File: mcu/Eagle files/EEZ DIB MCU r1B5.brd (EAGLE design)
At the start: 139 x 70 mm, 197 parts, among them IC1 TPD4E001DRLR, IC10 TPS61169DCKR, IC11 TPD4E001DRLR, IC12 TPA6205A1DGN, IC13 TPD4E001DRLR, IC14 TSC2007IPW, IC15 TPD4E001DRLR, IC16 DP83848CVV/NOPB, IC2 SN74LVC2G34DBVR, IC3 BTS3408G, IC4 STM32F769IGT6, IC5 LD1117ADT33TR, IC6 TPD4E001DRLR, IC7 IS42S16400J, IC8 AT24C256C-SSHL-B, IC9 TPS2051BDBVR, J1 503398-1892, J2 67803-8020, Q1 MMBT5551, SW1 TL1100CF160Q, SW2 PEC16-2215F-S0024, X1 ZL263-40DG, X2 ZL231-16KG, X3 1844249, X4 22-23-2061, X5 LMJTAB881243M-L, Y1 25MHz, Y2 XTAL016178-85SMX

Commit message: #44, #45 Eagle files
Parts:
- removed C67: 10u, EEZ_Lib1:EC1206
- removed C68, C69, C70, C71: 100n, rcl:C0603
- removed F1, F2: 50mA, EEZ_Lib1:F1210
- removed IC14: TSC2007IPW, EEZ_Lib1:PW(R-PDSO-G16)
- removed IC15: TPD4E001DRLR, EEZ_Lib1:DRL6
- removed IC16: DP83848CVV/NOPB, EEZ_Lib1:PT48
- removed R50, R53, R54, R56: 2K2, rcl:R0805
- removed R51, R52: 220R, rcl:R0805
- removed R55: 4K87, rcl:R0805
- removed ZD2: SMAJ18A, EEZ_Lib1:DO214AC
- removed ZD3: BZX384-B30.115, EEZ_Lib1:SOD323-W
- added Q2: 2N7002, EEZ_Lib1:SOT103P240X110-3N
- C11: value 18p -> EEEFK1V470P; device rcl:C0603 -> EEZ_Lib1:CAPAE660X610N
- C12: value 4p7 -> 100n
- C13: value EEEFK1V470P -> 4u7; device EEZ_Lib1:CAPAE660X610N -> EEZ_Lib1:EC1206
- C15: value 4u7 -> 100n; device EEZ_Lib1:EC1206 -> rcl:C0603
- C2, C5: value 100n -> 10n; device rcl:C0603 -> rcl:C0805
- C20: value 100n -> 4u7; device rcl:C0603 -> EEZ_Lib1:EC1206
- C22: value 4u7 -> 1u; device EEZ_Lib1:EC1206 -> rcl:C0805
- C23, C52: value 100n -> N.C.
- C24, C33, C58: value 1u -> 100n; device rcl:C0805 -> rcl:C0603
- C25: value N.C. -> 100n
- C31, C32, C46: value 100n -> 1u; device rcl:C0603 -> rcl:C0805
- C34, C48: value 1u -> 2u2
- C35: value 100n -> 2u2; device rcl:C0603 -> rcl:C0805
- C36: value 2u2 -> N.C.; device rcl:C0805 -> rcl:C0603
- C37: value 2u2 -> 4u7; device rcl:C0805 -> rcl:C1206
- C39, C53: value 4u7 -> 100n; device rcl:C1206 -> rcl:C0603
- C4: value 10n -> 100n; device rcl:C0805 -> rcl:C0603
- C45: value 100n -> 4u7; device rcl:C0603 -> rcl:C1206
- C47: device rcl:C1206 -> EEZ_Lib1:EC1206
- C49: value 4u7 -> N.C.; device EEZ_Lib1:EC1206 -> rcl:C1210
- C50: value 2u2 -> 100n; device rcl:C0805 -> rcl:C0603
- C51: value N.C. -> 4u7; device rcl:C1210 -> rcl:C1206
- C54: value 470n -> 1u
- C55: value 470n -> N.C.; device rcl:C0805 -> rcl:C0603
- C59: value N.C. -> 100n; device rcl:C0805 -> rcl:C0603
- C62: value 100n -> 10u; device rcl:C0603 -> EEZ_Lib1:EC1206
- C7: value 10n -> 18p; device rcl:C0805 -> rcl:C0603
- C8: value 100n -> 4p7
- IC1: value TPD4E001DRLR -> CD74HC4050PWR; device EEZ_Lib1:DRL6 -> EEZ_DIB:PW16
- IC10: value TPS61169DCKR -> TPD4E001DRLR; device EEZ_Lib1:DCK5 -> EEZ_Lib1:DRL6
- IC11: value TPD4E001DRLR -> TSC2007IPW; device EEZ_Lib1:DRL6 -> EEZ_Lib1:PW(R-PDSO-G16)
- IC12: value TPA6205A1DGN -> TPD4E001DRLR; device EEZ_Lib1:SOP65P490X110-9N -> EEZ_Lib1:DRL6
- IC13: value TPD4E001DRLR -> DP83848CVV/NOPB; device EEZ_Lib1:DRL6 -> EEZ_Lib1:PT48
- IC2: value SN74LVC2G34DBVR -> STM32F769IGT6; device EEZ_Lib1:DBV6 -> EEZ_DIB:LQFP-176_24X24MM
- IC3: value BTS3408G -> LD1117ADT33TR; device EEZ_Lib1:SOIC127P600X173-8N -> v-reg:DPACK
- IC4: value STM32F769IGT6 -> TPD4E001DRLR; device EEZ_DIB:LQFP-176_24X24MM -> EEZ_Lib1:DRL6
- IC5: value LD1117ADT33TR -> IS42S16400J; device v-reg:DPACK -> EEZ_Lib1:TSOPII-54
- IC6: value TPD4E001DRLR -> AT24C256C-SSHL-B; device EEZ_Lib1:DRL6 -> EEZ_Lib1:SOIC127P600X173-8N
- IC7: value IS42S16400J -> TPS2051BDBVR; device EEZ_Lib1:TSOPII-54 -> EEZ_Lib1:DBV5
- IC8: value AT24C256C-SSHL-B -> TPS61169DCKR; device EEZ_Lib1:SOIC127P600X173-8N -> EEZ_Lib1:DCK5
- IC9: value TPS2051BDBVR -> TPD4E001DRLR; device EEZ_Lib1:DBV5 -> EEZ_Lib1:DRL6
- Q1: value MMBT5551 -> N.C.
- R18: value 10K -> N.C.
- R19, R20: value 22R -> N.C.
- R2: value 4K7 -> 10K
- R25: value 330R -> N.C.
- R28: value 47K -> N.C.
- R32: value 10K -> 1K5
- R33, R34, R37: value 10K -> 49R9
- R35, R38: value 10K -> 2K2
- R36: value 47K -> 2K2
- R39: value 1K5 -> N.C.
- R4, R8: value 1K -> 4K7
- R40, R41, R49: value 49R9 -> 2K2
- R42: value 2K2 -> 49R9
- R44: value 49R9 -> 220R
- R45: value 2K2 -> 220R
- R46: value 220R -> 2K2
- R48: value 2K2 -> 4K87
- R5: value 10K -> 1K
- R9: value 4K7 -> 1K
- SP1: value LD-BZEL-M1313 -> AI-1223-TWT or LD-BZEN 0903; device EEZ_Lib1:LD-BZEL-M1313 -> EEZ_Lib1:AI-1223-TWT_COMBO
- SPEED: value LTST-C170YKT -> N.C.
- VBUS: value HSMG-C170 -> N.C.
- X4: value 22-23-2061 -> N.C.
- ZD1: value SMAJ18A -> BZX384-B30.115; device EEZ_Lib1:DO214AC -> EEZ_Lib1:SOD323-W
- moved R36 95.1 mm to (3.37, 31.8)
- moved R33 94.0 mm to (8.83, 47.0), turned to 270 degrees
- moved R32 91.5 mm to (9.27, 31.8)
- moved IC12 90.6 mm to (11.1, 21.6)
- moved C59 90.1 mm to (6.55, 21.2)
- moved R37 87.7 mm to (12.8, 47.0), turned to 270 degrees
- moved R38 87.0 mm to (14.1, 25.7), turned to 0 degrees
- moved C4 86.2 mm to (31.6, 15.3), turned to 270 degrees
- moved R34 85.9 mm to (10.8, 47.0), turned to 90 degrees
- moved C55 83.2 mm to (13.9, 22.6), turned to 0 degrees
- moved R35 78.1 mm to (18.1, 25.7)
- moved R6 77.6 mm to (104.6, 16.6), turned to 270 degrees
- moved R9 77.0 mm to (28.0, 25.2), turned to 90 degrees
- moved C2 75.6 mm to (102.6, 16.6), turned to 270 degrees
- moved R2 74.0 mm to (98.0, 16.6), turned to 270 degrees
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- renumbered BOOT0 to BOOT1
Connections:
- removed net !AUDIO_SHDN: IC12.1, R36.1
- removed net N$166: IC12.8, R33.1, SP1.-
- removed net N$171: IC12.4, R35.1, R37.2
- removed net N$181: IC12.3, R32.2, R34.1
- removed net N$193: C54.1, R34.2
- removed net N$194: C59.2, IC12.2
- removed net N$195: C55.1, R35.2
- removed net N$44: F1.1, X3.4
- removed net N$45: F2.1, X3.5
- removed net N$50: IC12.5, R38.1, SP1.+
- removed net N$6: R37.1, R38.2
- net !FAULT: now also IC2.58; no longer IC3.1, IC4.58
- net !RESET: now also IC13.29, IC2.31, IC4.4; no longer IC16.29, IC3.4, IC4.31, IC6.4
- net !USB_OTG_FS_OC: now also IC2.146, IC7.3; no longer IC4.146, IC9.3
- net +3V3: now also C13.+, C36.1, C37.1, C38.2, C4.1, C40.1, C48.1, C52.2, C53.2, C54.2, C55.1, C65.1, C66.1, IC1.1, IC10.6, IC11.1, IC12.6, IC13.32, IC13.48, IC3.4, IC4.6, IC5.1, IC5.14, IC5.27, IC5.3, IC5.43, IC5.49, IC5.9, IC6.8, R32.2, R36.1, R39.1, R40.1, R41.1, R49.1, R6.1; no longer C15.+, C38.1, C40.2, C45.1, C46.1, C5.1, C50.1, C56.2, C57.2, C58.2, C60.1, C70.1, C71.1, IC13.6, IC14.1, IC15.6, IC16.32, IC16.48, IC2.5, IC5.4, IC6.6, IC7.1, IC7.14, IC7.27, IC7.3, IC7.43, IC7.49, IC7.9, IC8.8, R36.2, R39.2, R48.1, R50.1, R53.1, R54.1, R56.1, R9.1
- net +3V3(A): now also C57.2, C59.2, C64.1, IC13.22; no longer C62.2, C64.2, C69.1, IC16.22
- net +5V: now also C11.1, C12.1, C45.1, IC3.3, IC7.5; no longer C13.1, C14.1, C2.1, C47.1, C8.2, IC1.6, IC3.8, IC5.3, IC9.5
- net BOOT0: now also IC2.166; no longer IC4.166
- net BYPASS_REG: now also IC2.48; no longer IC4.48
- net DAC_OUT1: now also IC2.50, Q2.1; no longer C55.2, IC4.50
- net DIN2: now also IC2.8, R9.2; no longer IC4.8, R8.2
- net DOUT2: now also IC1.7, IC1.9, IC2.163; no longer IC3.3, IC4.163
- net ENC_A: now also C5.2, IC2.119, R2.1; no longer C6.2, IC4.119, R5.1
- net ENC_B: now also C6.1, IC2.120; no longer C7.1, IC4.120
- net ENC_SW: now also C2.2, IC2.173; no longer C3.2, IC4.173
- net EOUT_A: now also R6.2; no longer R9.2
- net EOUT_B: now also R2.2; no longer R5.2
- net ETH_COL: now also IC2.47; no longer IC4.47
- net ETH_CRS: now also IC2.40; no longer IC4.40
- net ETH_MDC: now also IC13.31, IC2.33; no longer IC16.31, IC4.33
- net ETH_MDIO: now also IC13.30, IC2.42, R32.1; no longer IC16.30, IC4.42, R39.1
- net ETH_RXD0: now also IC2.54; no longer IC4.54
- net ETH_RXD1: now also IC2.55; no longer IC4.55
- net ETH_RXD2: now also IC2.83; no longer IC4.83
- net ETH_RXD3: now also IC2.84; no longer IC4.84
- net ETH_RX_CLK: now also IC2.41; no longer IC4.41
- net ETH_RX_DV: now also IC2.53; no longer IC4.53
- net ETH_RX_ERR: now also IC2.79; no longer IC4.79
- net ETH_TXD0: now also IC2.85; no longer IC4.85
- net ETH_TXD1: now also IC2.86; no longer IC4.86
- net ETH_TXD2: now also IC2.34; no longer IC4.34
- net ETH_TXD3: now also IC2.167; no longer IC4.167
- net ETH_TX_CLK: now also IC2.35; no longer IC4.35
- net ETH_TX_EN: now also IC2.80; no longer IC4.80
- net FMC_A0: now also IC2.16, IC5.23; no longer IC4.16, IC7.23
- net FMC_A1: now also IC2.17, IC5.24; no longer IC4.17, IC7.24
- net FMC_A10: now also IC2.66, IC5.22; no longer IC4.66, IC7.22
- net FMC_A11: now also IC2.67, IC5.35; no longer IC4.67, IC7.35
- net FMC_A2: now also IC2.18, IC5.25; no longer IC4.18, IC7.25
- net FMC_A3: now also IC2.19, IC5.26; no longer IC4.19, IC7.26
- net FMC_A4: now also IC2.20, IC5.29; no longer IC4.20, IC7.29
- net FMC_A5: now also IC2.21, IC5.30; no longer IC4.21, IC7.30
- net FMC_A6: now also IC2.60, IC5.31; no longer IC4.60, IC7.31
- net FMC_A7: now also IC2.63, IC5.32; no longer IC4.63, IC7.32
- net FMC_A8: now also IC2.64, IC5.33; no longer IC4.64, IC7.33
- net FMC_A9: now also IC2.65, IC5.34; no longer IC4.65, IC7.34
- net FMC_BA0: now also IC2.112, IC5.20; no longer IC4.112, IC7.20
- net FMC_BA1: now also IC2.113, IC5.21; no longer IC4.113, IC7.21
- net FMC_D0: now also IC2.97, IC5.2; no longer IC4.97, IC7.2
- net FMC_D1: now also IC2.98, IC5.4; no longer IC4.98, IC7.4
- net FMC_D10: now also IC2.76, IC5.45; no longer IC4.76, IC7.45
- net FMC_D11: now also IC2.77, IC5.47; no longer IC4.77, IC7.47
- net FMC_D12: now also IC2.78, IC5.48; no longer IC4.78, IC7.48
- net FMC_D13: now also IC2.89, IC5.50; no longer IC4.89, IC7.50
- net FMC_D14: now also IC2.90, IC5.51; no longer IC4.90, IC7.51
- net FMC_D15: now also IC2.91, IC5.53; no longer IC4.91, IC7.53
- net FMC_D2: now also IC2.142, IC5.5; no longer IC4.142, IC7.5
- net FMC_D3: now also IC2.143, IC5.7; no longer IC4.143, IC7.7
- net FMC_D4: now also IC2.68, IC5.8; no longer IC4.68, IC7.8
- net FMC_D5: now also IC2.69, IC5.10; no longer IC4.69, IC7.10
- net FMC_D6: now also IC2.70, IC5.11; no longer IC4.70, IC7.11
- net FMC_D7: now also IC2.73, IC5.13; no longer IC4.73, IC7.13
- net FMC_D8: now also IC2.74, IC5.42; no longer IC4.74, IC7.42
- net FMC_D9: now also IC2.75, IC5.44; no longer IC4.75, IC7.44
- net FMC_NBL0: now also IC2.169, IC5.15; no longer IC4.169, IC7.15
- net FMC_NBL1: now also IC2.170, IC5.39; no longer IC4.170, IC7.39
- net FMC_SDCKE0: now also IC2.43, IC5.37; no longer IC4.43, IC7.37
- net FMC_SDCLK: now also IC2.116, IC5.38; no longer IC4.116, IC7.38
- net FMC_SDNCAS: now also IC2.160, IC5.17; no longer IC4.160, IC7.17
- net FMC_SDNE0: now also IC2.44, IC5.19; no longer IC4.44, IC7.19
- net FMC_SDNRAS: now also IC2.59, IC5.18; no longer IC4.59, IC7.18
- net FMC_SDNWE: now also IC2.46, IC5.16; no longer IC4.46, IC7.16
- net GND: now also C11.2, C13.-, C15.2, C2.1, C20.-, C22.2, C38.1, C4.2, C40.2, C47.-, C49.2, C5.1, C50.1, C51.1, C54.1, C55.2, C56.2, C58.2, C6.2, C62.-, C64.2, C7.1, C8.2, IC1.8, IC10.3, IC11.13, IC11.14, IC11.6, IC12.3, IC13.15, IC13.19, IC13.35, IC13.36, IC13.47, IC2.103, IC2.109, IC2.117, IC2.130, IC2.135, IC2.14, IC2.148, IC2.158, IC2.22, IC2.37, IC2.61, IC2.71, IC2.95, IC3.1, IC4.3, IC5.12, IC5.28, IC5.41, IC5.46, IC5.52, IC5.54, IC5.6, IC6.1, IC6.2, IC6.4, IC6.7, IC7.2, IC9.3, Q2.2, R35.1, R38.1, R48.1; no longer C11.1, C13.2, C15.-, C2.2, C20.2, C22.-, C38.2, C4.1, C40.1, C47.2, C49.-, C5.2, C50.2, C51.2, C54.2, C56.1, C58.1, C6.1, C62.1, C64.1, C67.-, C68.2, C69.2, C7.2, C70.2, C71.2, C8.1, IC1.3, IC10.2, IC11.3, IC12.7, IC12.TP, IC13.3, IC14.13, IC14.14, IC14.6, IC15.3, IC16.15, IC16.19, IC16.35, IC16.36, IC16.47, IC2.2, IC3.6, IC4.103, IC4.109, IC4.117, IC4.130, IC4.135, IC4.14, IC4.148, IC4.158, IC4.22, IC4.37, IC4.61, IC4.71, IC4.95, IC5.1, IC7.12, IC7.28, IC7.41, IC7.46, IC7.52, IC7.54, IC7.6, IC8.1, IC8.3, IC8.4, IC8.7, IC9.2, R42.1, R45.1, R55.1, ZD1.A, ZD2.A
- net I2C1_SCL: now also IC11.12, IC2.164, IC6.6; no longer IC14.12, IC4.164, IC8.6
- net I2C1_SDA: now also IC11.11, IC2.165, IC6.5; no longer IC14.11, IC4.165, IC8.5
- net IRQ_TOUCH: now also IC11.10, IC2.151; no longer IC14.10, IC4.151
- net LED_ACT: now also IC13.26, R36.2, R44.2; no longer IC16.26, R43.2, R51.2
- net LED_LINK: now also IC13.28, R43.2, R45.2; no longer IC16.28, R50.2, R52.2
- net LED_SPEED: now also IC13.27, R41.2; no longer IC16.27, R48.2
- net LTDC_B2: now also IC2.150; no longer IC4.150
- net LTDC_B3: now also IC2.154; no longer IC4.154
- net LTDC_B4: now also IC2.155; no longer IC4.155
- net LTDC_B5: now also IC2.174; no longer IC4.174
- net LTDC_B6: now also IC2.175; no longer IC4.175
- net LTDC_B7: now also IC2.176; no longer IC4.176
- net LTDC_CLK: now also IC2.115; no longer IC4.115
- net LTDC_DE: now also IC2.28; no longer IC4.28
- net LTDC_G2: now also IC2.52; no longer IC4.52
- net LTDC_G3: now also IC2.153; no longer IC4.153
- net LTDC_G4: now also IC2.45; no longer IC4.45
- net LTDC_G5: now also IC2.132; no longer IC4.132
- net LTDC_G6: now also IC2.13; no longer IC4.13
- net LTDC_G7: now also IC2.145; no longer IC4.145
- net LTDC_HSYNC: now also IC2.12; no longer IC4.12
- net LTDC_R2: now also IC2.139; no longer IC4.139
- net LTDC_R3: now also IC2.56; no longer IC4.56
- net LTDC_R4: now also IC2.51; no longer IC4.51
- net LTDC_R5: now also IC2.32; no longer IC4.32
- net LTDC_R6: now also IC2.57; no longer IC4.57
- net LTDC_R7: now also IC2.114; no longer IC4.114
- net LTDC_VSYNC: now also IC2.11; no longer IC4.11
- net MCLK_25: now also IC2.122; no longer IC4.122
- net N$1: now also IC13.1; no longer IC16.1
- net N$10: now also IC13.2; no longer IC16.2
- net N$101: now also R39.2; no longer R46.2
- net N$102: now also C58.1, R37.1, R42.2; no longer C63.1, R44.1, R49.2
- net N$11: now also IC13.39; no longer IC16.39
- net N$12: now also IC13.38; no longer IC16.38
- net N$15: now also IC13.3; no longer IC16.3
- net N$17: now also IC13.4; no longer IC16.4
- net N$178: now also IC2.100, IC2.106; no longer IC4.100, IC4.106
- net N$21: now also IC13.5; no longer IC16.5
- net N$22: now also IC13.34; no longer IC16.34
- net N$23: now also R40.2; no longer R47.2
- net N$25: now also R38.2; no longer R45.2
- net N$26: now also R35.2; no longer R42.2
- net N$27: now also IC13.7; no longer IC16.7
- net N$28: now also R49.2; no longer R56.2
- net N$29: now also IC13.6; no longer IC16.6
- net N$3: now also C56.1, R33.1, R34.2; no longer C61.1, R40.1, R41.2
- net N$30: now also IC8.5; no longer IC10.5
- net N$31: now also IC13.46; no longer IC16.46
- net N$32: now also IC13.45; no longer IC16.45
- net N$33: now also IC13.42; no longer IC16.42
- net N$34: now also IC13.44; no longer IC16.44
- net N$35: now also IC13.43; no longer IC16.43
- net N$36: now also IC13.41; no longer IC16.41
- net N$37: now also IC13.40; no longer IC16.40
- net N$38: now also R3.2, R4.1; no longer R2.2, R3.1
- net N$39: now also R3.1; no longer R2.1
- net N$40: now also R7.1; no longer R6.1
- net N$41: now also R7.2, R8.1; no longer R6.2, R7.1
- net N$42: now also IC1.15, R5.1; no longer IC2.6, R4.1
- net N$43: now also IC1.2, R9.1; no longer IC2.4, R8.1
- net N$46: now also IC1.14, R4.2; no longer IC1.1, IC2.1, R3.2
- net N$47: now also IC1.3, R8.2; no longer IC1.2, IC2.3, R7.2
- net N$48: now also IC1.12, X3.4; no longer F1.2, IC3.7, ZD1.C
- net N$49: now also IC1.10, IC1.6, X3.5; no longer F2.2, IC1.5, IC3.5, ZD2.C
- net N$5: now also Q2.3, SP1.-B, SP1.-B.1; no longer R32.1, R33.2
- net N$52: now also C51.2, SP1.+B, SP1.+B.1; no longer C53.2, IC12.6
- net N$8: now also R44.1; no longer R51.1
- net N$9: now also R45.1; no longer R52.1
- net N$97: now also IC13.24, R48.2; no longer IC16.24, R55.2
- net N$98: now also IC13.21, R46.2; no longer IC16.21, R53.2
- net N$99: now also IC13.20, R47.2; no longer IC16.20, R54.2
- net OE_SYNC: now also IC2.94; no longer IC4.94
- net PE: now also C49.1; no longer C51.1
- net PFBOUT: now also C60.1, C61.1, C62.+, C63.1, IC13.18, IC13.23, IC13.37; no longer C65.1, C66.1, C67.+, C68.1, IC16.18, IC16.23, IC16.37
- net PWR_DIRECT: now also IC2.110; no longer IC4.110
- net PWR_SSTART: now also IC2.111; no longer IC4.111
- net RCC_OSC32_IN: now also C8.1, IC2.9; no longer C10.1, IC4.9
- net RCC_OSC32_OUT: now also C10.1, IC2.10; no longer C12.1, IC4.10
- net RCC_OSC_IN: now also C7.2, IC2.29; no longer C9.2, IC4.29
- net RCC_OSC_OUT: now also C9.2, IC2.30; no longer C11.2, IC4.30
- net RD+: now also IC12.4, IC13.14, R37.2; no longer IC15.4, IC16.14, R44.2
- net RD-: now also IC12.5, IC13.13, R42.1; no longer IC15.5, IC16.13, R49.1
- net SDMMC1_CK: now also IC2.141; no longer IC4.141
- net SDMMC1_CMD: now also IC2.144; no longer IC4.144
- net SDMMC1_D0: now also IC2.121; no longer IC4.121
- net SD_DETECT: now also IC2.140; no longer IC4.140
- net SPI2_CLK: now also IC2.133; no longer IC4.133
- net SPI2_CSA: now also IC2.93; no longer IC4.93
- net SPI2_CSB: now also IC2.92; no longer IC4.92
- net SPI2_IRQ: now also IC2.123; no longer IC4.123
- net SPI2_MISO: now also IC2.87; no longer IC4.87
- net SPI2_MOSI: now also IC2.134; no longer IC4.134
- net SPI4_CLK: now also IC2.1; no longer IC4.1
- net SPI4_CSA: now also IC2.2; no longer IC4.2
- net SPI4_CSB: now also IC2.3; no longer IC4.3
- net SPI4_IRQ: now also IC2.168; no longer IC4.168
- net SPI4_MISO: now also IC2.4; no longer IC4.4
- net SPI4_MOSI: now also IC2.5; no longer IC4.5
- net SPI5_CLK: now also IC2.25; no longer IC4.25
- net SPI5_CSA: now also IC2.157; no longer IC4.157
- net SPI5_CSB: now also IC2.156; no longer IC4.156
- net SPI5_IRQ: now also IC2.138; no longer IC4.138
- net SPI5_MISO: now also IC2.26; no longer IC4.26
- net SPI5_MOSI: now also IC2.27; no longer IC4.27
- net SW_WLED: now also IC8.1; no longer IC10.1
- net SYS_JTCK-SWCLK: now also IC2.137; no longer IC4.137
- net SYS_JTDO-SWO: now also IC2.161, IC4.5; no longer IC4.161, IC6.5
- net SYS_JTMS-SWDIO: now also IC2.128; no longer IC4.128
- net TCK: now also IC4.1; no longer IC6.1
- net TD+: now also IC12.1, IC13.17, R33.2; no longer IC15.1, IC16.17, R40.2
- net TD-: now also IC12.2, IC13.16, R34.1; no longer IC15.2, IC16.16, R41.1
- net TFT_BRIGHTNESS: now also IC2.88, IC8.4; no longer IC10.4, IC4.88
- net TMS: now also IC4.2; no longer IC6.2
- net UART_RX/DIN1: now also IC2.24, R5.2; no longer IC4.24, R4.2
- net UART_TX/DOUT1: now also IC1.11, IC1.5, IC2.162; no longer IC3.2, IC4.162
- net USB_D_N: now also IC9.1; no longer IC11.1
- net USB_D_P: now also IC9.2; no longer IC11.2
- net USB_OTG_FS_D_N: now also IC2.126; no longer IC4.126
- net USB_OTG_FS_D_P: now also IC2.127; no longer IC4.127
- net USB_OTG_FS_ID: now also IC2.125, IC9.4; no longer IC11.4, IC4.125
- net USB_OTG_FS_PSO: now also IC2.147, IC7.4; no longer IC4.147, IC9.4
- net USB_OTG_FS_VBUS: now also C47.+, C50.2, IC2.124, IC7.1, IC9.6; no longer C49.+, C52.2, IC11.6, IC4.124, IC9.1
- net USER_SW: now also C3.2, IC2.152; no longer C4.2, IC4.152
- net VBAT: now also IC2.6; no longer IC4.6
- net VCAP1: now also C35.1, IC2.81; no longer C37.1, IC4.81
- net VCAP2: now also C34.1, IC2.129; no longer C36.1, IC4.129
- net VDD: now also C14.1, C15.1, C20.+, C22.1, IC2.118, IC2.131, IC2.136, IC2.149, IC2.15, IC2.159, IC2.171, IC2.172, IC2.23, IC2.36, IC2.49, IC2.62, IC2.72, IC2.82, IC2.96, IC2.99; no longer C20.1, C22.+, C32.1, C33.1, IC4.118, IC4.131, IC4.136, IC4.149, IC4.15, IC4.159, IC4.171, IC4.172, IC4.23, IC4.36, IC4.49, IC4.62, IC4.72, IC4.82, IC4.96, IC4.99
- net VDDA: now also C32.1, C33.1, IC2.39; no longer C34.1, C35.1, IC4.39
- net VLED+: now also C46.1, ZD1.C; no longer C48.1, ZD3.C
- net VLED-: now also IC8.3, ZD1.A; no longer IC10.3, ZD3.A
- net VREF+: now also IC2.38; no longer IC4.38
- net XL: now also IC10.4, IC11.4; no longer IC13.4, IC14.4
- net XR: now also IC10.1, IC11.2; no longer IC13.1, IC14.2
- net YD: now also IC10.2, IC11.5; no longer IC13.2, IC14.5
- net YU: now also IC10.5, IC11.3; no longer IC13.5, IC14.3
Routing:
- net !FAULT: track 225.5 -> 197.4 mm, vias 8 -> 6
- net N$50: track 17.6 -> 0.00 mm, vias 2 -> 0
- net N$166: track 15.4 -> 0.00 mm
- net GND: track 151.2 -> 139.6 mm, vias 155 -> 142
- net +5V: track 247.8 -> 239.2 mm, vias 7 -> 5
- net N$171: track 8.43 -> 0.00 mm, vias 2 -> 0
- net UART_TX/DOUT1: track 142.2 -> 149.7 mm
- net N$5: track 1.98 -> 9.27 mm
- net N$181: track 7.16 -> 0.00 mm
- net N$44: track 5.42 -> 0.00 mm
- net !RESET: track 238.1 -> 233.7 mm, vias 14 -> 13
- net DOUT2: track 77.8 -> 82.1 mm
- net N$45: track 3.66 -> 0.00 mm
- net N$47: track 11.5 -> 8.40 mm
- net N$195: track 2.76 -> 0.00 mm
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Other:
- board text added: "EEZ DIB MCU (07/2019 r1B5)"
- board text removed: "EEZ DIB MCU (07/2019 r1B4)"

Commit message: #46
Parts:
- removed JP2, JP3: JP2-CUT, EEZ_Lib1:JP2-CUT
- added SCL, SDA: JP2-NOCUT, EEZ_Lib1:JP2-NOCUT
- C1, C49: device rcl:C1210 -> rcl:C0805
- X2: device EEZ_connectors:ML16L -> EEZ_connectors:IDC-16PIN
- moved X2 27.6 mm to (0.00, 48.9), turned to 270 degrees
- moved C11 18.6 mm to (24.5, 65.2), turned to 0 degrees
- moved C12 16.1 mm to (26.7, 60.7), turned to 0 degrees
- moved D1 15.9 mm to (7.04, 53.6), turned to 270 degrees
- moved IC3 15.7 mm to (18.4, 58.5)
- moved JP1 8.94 mm to (6.55, 59.2)
- moved FM2 8.69 mm to (113.1, 67.8)
- moved R46 8.68 mm to (10.2, 52.3)
- moved R47 8.68 mm to (12.2, 52.3)
- moved C1 8.63 mm to (7.49, 61.4)
- moved C56 6.54 mm to (13.5, 47.4)
- moved C13 5.74 mm to (11.5, 58.9), turned to 90 degrees
- moved R49 4.72 mm to (21.4, 52.2), turned to 270 degrees
- moved FB2 4.69 mm to (6.15, 45.7), turned to 270 degrees
- moved C36 3.71 mm to (99.4, 66.5), turned to 0 degrees
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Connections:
- net I2C1_SCL: now also SCL.1; no longer JP2.1
- net I2C1_SDA: now also SDA.2; no longer JP3.2
- net N$13: now also SDA.1; no longer JP3.1
- net N$7: now also SCL.2; no longer JP2.2
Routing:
- net N$7: track 49.8 -> 102.6 mm
- net N$13: track 49.6 -> 102.1 mm
- net PWR_SSTART: track 67.5 -> 110.0 mm
- net +VAUX: track 147.8 -> 188.1 mm
- net PWR_DIRECT: track 68.8 -> 108.0 mm
- net !FAULT: track 197.4 -> 231.8 mm, vias 6 -> 7
- net BOOT0: track 100.3 -> 115.2 mm
- net PE: track 182.3 -> 172.5 mm
- net +5V: track 239.2 -> 246.0 mm, vias 5 -> 11
- net N$99: track 7.92 -> 12.3 mm
- net N$27: track 4.18 -> 7.33 mm
- net LED_SPEED: track 11.9 -> 14.9 mm
- net N$98: track 9.62 -> 12.4 mm
- net +3V3: track 91.1 -> 93.6 mm, vias 66 -> 53
- net N$97: track 5.37 -> 7.77 mm
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- removed copper zone on layer 16, net +3V3
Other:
- board size 139 x 70 mm -> 139.5 x 70 mm

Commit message: MCU board BOM update
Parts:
- moved FM2 0.36 mm to (113.0, 67.5)
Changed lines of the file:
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@@
 <setting verticaltext="up"/>
 </settings>
-<grid distance="0.5" unitdist="mil" unit="mil" style="lines" multiple="10" display="no" altdistance="12.5" altunitdist="mil" altunit="mil"/>
+<grid distance="0.0127" unitdist="mm" unit="mm" style="lines" multiple="10" display="no" altdistance="12.5" altunitdist="mil" altunit="mil"/>
 <layers>
 <layer number="1" name="Top" color="11" fill="1" visible="yes" active="yes"/>
@@
 <layer number="13" name="Route13" color="4" fill="5" visible="no" active="no"/>
 <layer number="14" name="Route14" color="1" fill="6" visible="no" active="no"/>
-<layer number="15" name="Power" color="6" fill="1" visible="yes" active="yes"/>
+<layer number="15" name="Power" color="6" fill="1" visible="no" active="yes"/>
 <layer number="16" name="Bottom" color="1" fill="1" visible="yes" active="yes"/>
 <layer number="17" name="Pads" color="6" fill="1" visible="yes" active="yes"/>
@@
 <element name="U$6" library="olimex_logo1" package="ESD_SYMBOL" value="" x="106.0686" y="22.0788" smashed="yes"/>
 <element name="FM1" library="EEZ_Lib1" package="FIDUCIAL" value="FIDUCIAL" x="-1.5" y="9" smashed="yes"/>
-<element name="FM2" library="EEZ_Lib1" package="FIDUCIAL" value="FIDUCIAL" x="113.142" y="67.834" smashed="yes"/>
+<element name="FM2" library="EEZ_Lib1" package="FIDUCIAL" value="FIDUCIAL" x="113" y="67.5" smashed="yes"/>
 <element name="Y1" library="EEZ_Lib1" package="HC-49/4H" value="25MHz" x="51.816" y="60.198" smashed="yes">
 <attribute name="NAME" x="44.4787" y="61.3664" size="1.016" layer="25" ratio="10"/>

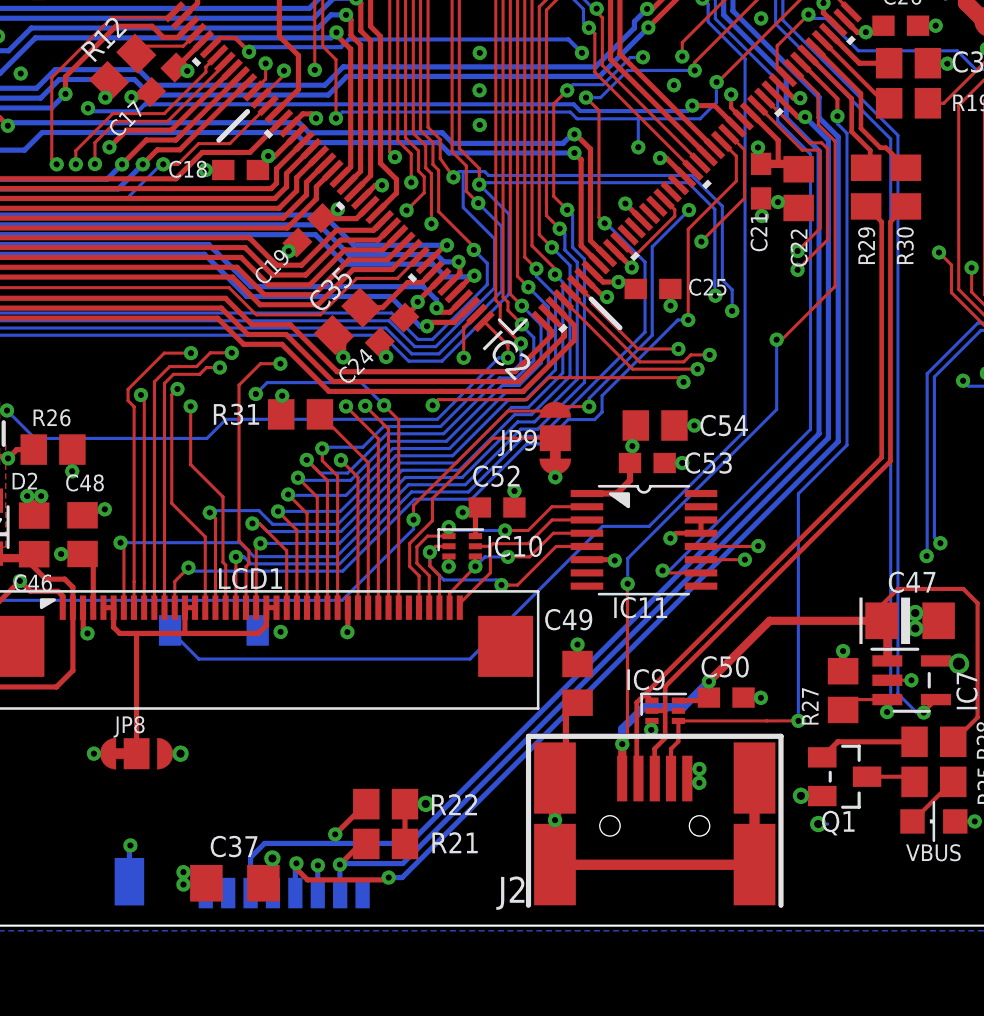
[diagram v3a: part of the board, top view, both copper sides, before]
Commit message: MCU J1 update
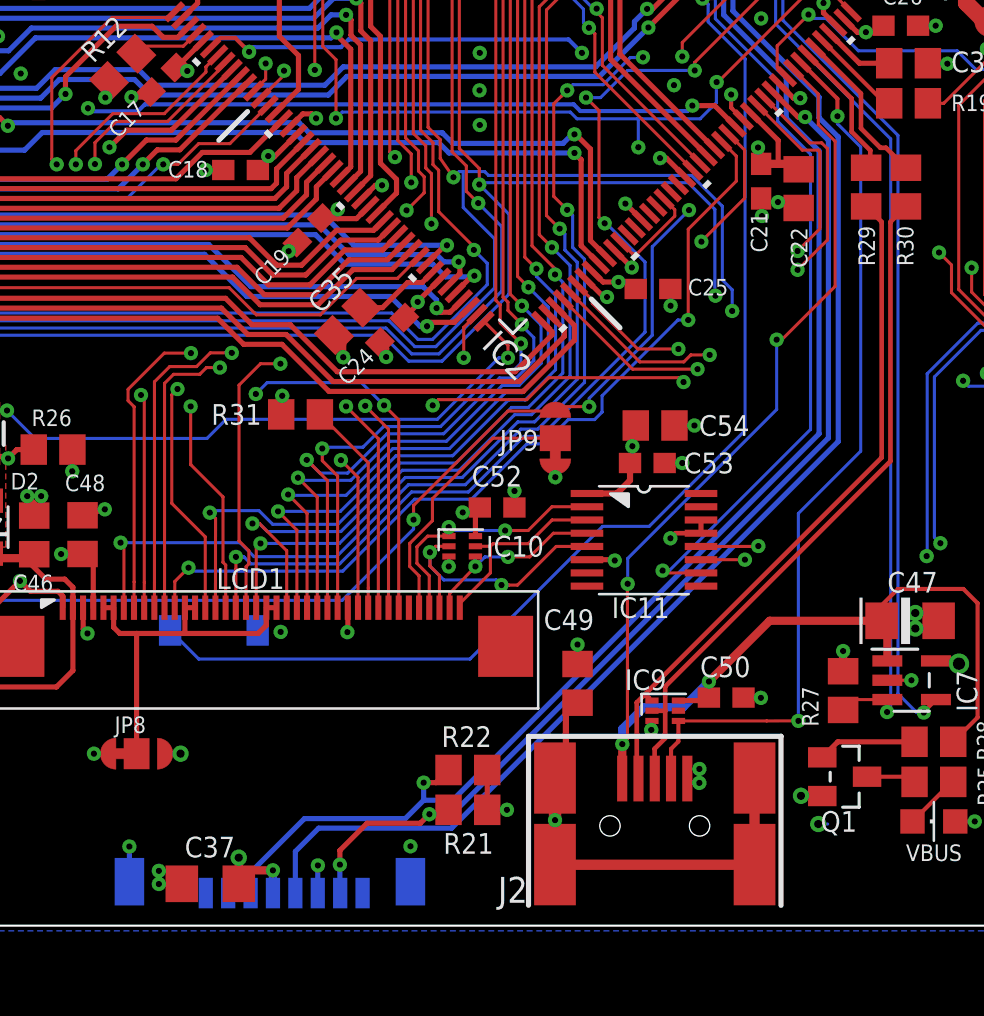
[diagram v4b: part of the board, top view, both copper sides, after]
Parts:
- moved R21 4.37 mm to (67.3, 5.69)
- moved R22 4.37 mm to (67.3, 7.65)
- moved C37 1.21 mm to (54.7, 2.06)
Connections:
- net GND: now also J1.S1
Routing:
- net +3V3: track 93.6 -> 94.5 mm, vias 53 -> 54
- net SDMMC1_CMD: track 71.4 -> 70.7 mm
- net USB_OTG_FS_ID: track 43.1 -> 43.7 mm
- net SDMMC1_CK: track 67.6 -> 67.2 mm, vias 3 -> 1
- net SDMMC1_D0: track 54.2 -> 53.9 mm, vias 2 -> 3
- net GND: vias 143 -> 144

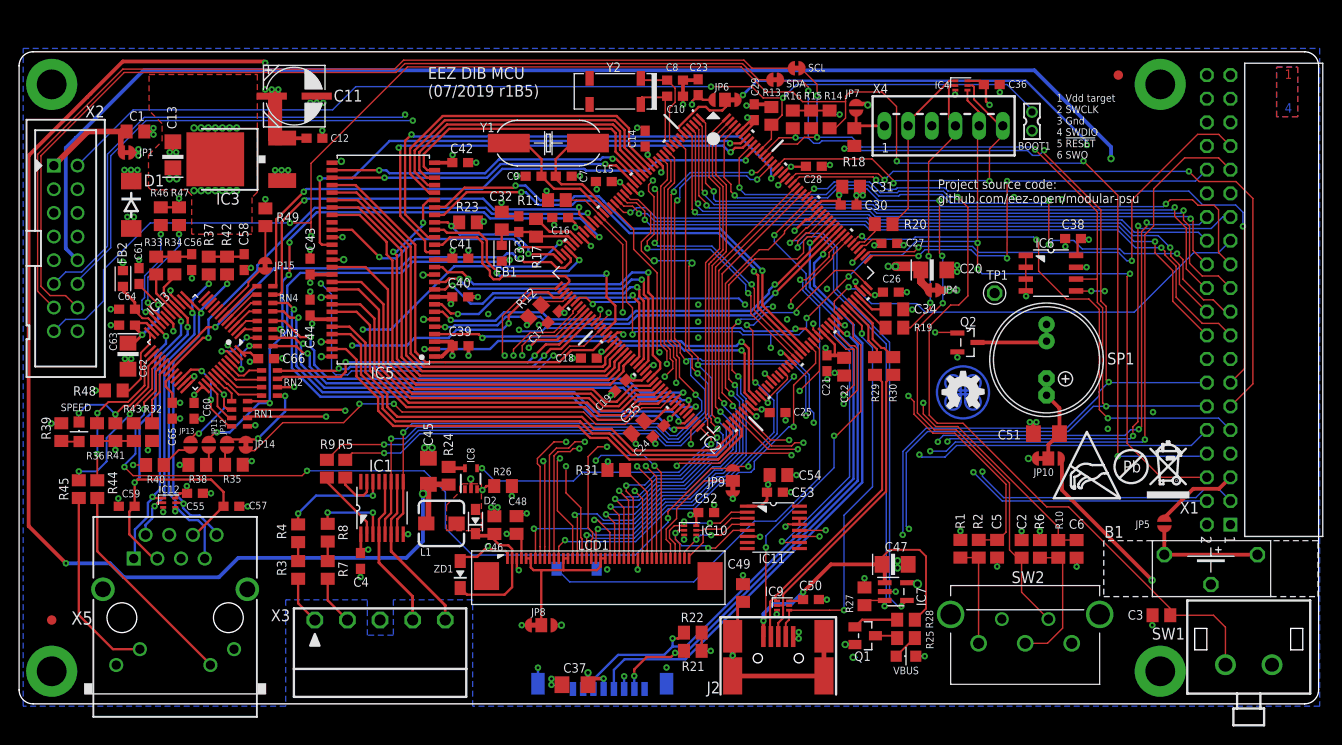
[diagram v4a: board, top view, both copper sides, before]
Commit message: MCU optional I/O protection
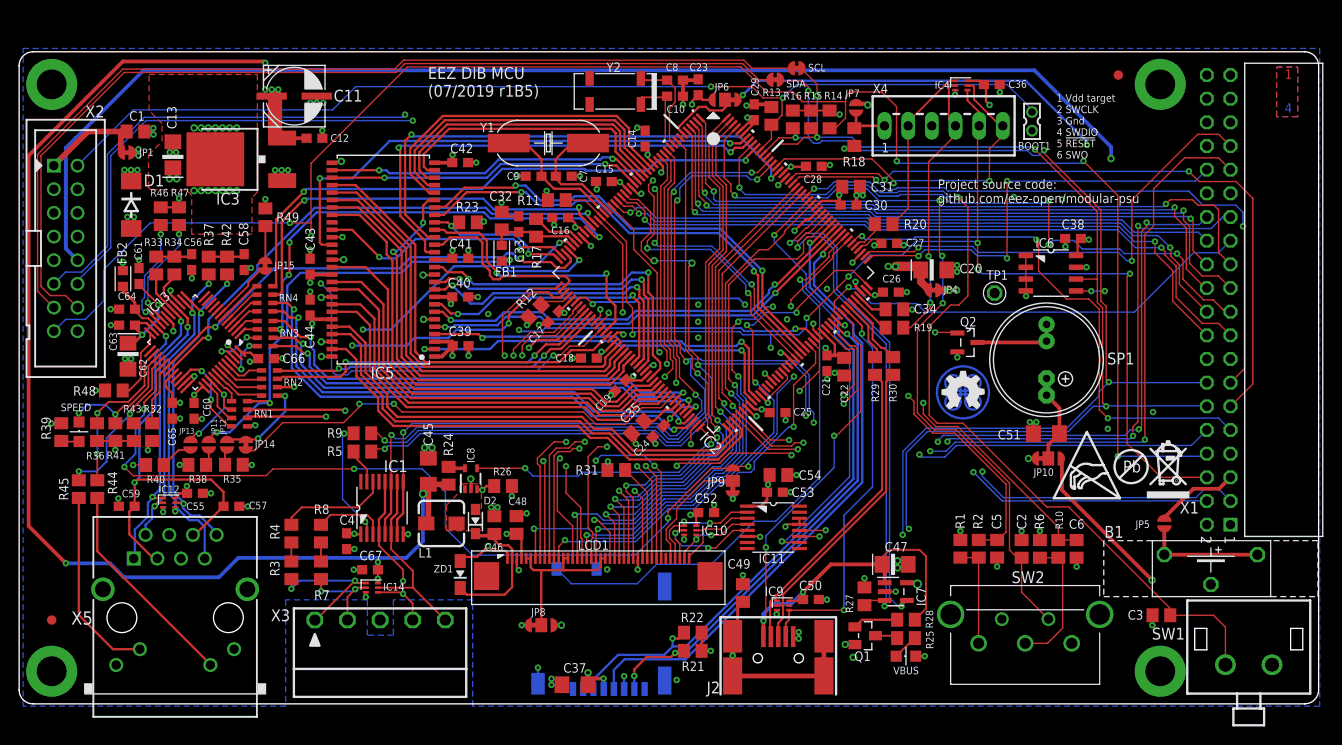
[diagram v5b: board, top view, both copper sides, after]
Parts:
- added C67: N.C., rcl:C0603
- added IC14: TPD4E001DRLR, EEZ_Lib1:DRL6
- moved R9 5.38 mm to (31.9, 29.0), turned to 0 degrees
- moved R5 2.60 mm to (31.9, 27.1), turned to 0 degrees
- moved C4 2.59 mm to (30.2, 17.5)
- moved R8 0.73 mm to (27.4, 18.3)
- moved R3 0.72 mm to (24.2, 14.3)
- moved R4 0.72 mm to (24.2, 18.3)
- moved R7 0.72 mm to (27.4, 14.3)
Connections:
- removed net N$39: R3.1, X3.1
- removed net N$40: R7.1, X3.2
- new net N$14: IC14.2, R7.1, X3.2
- new net N$6: IC14.1, R3.1, X3.1
- net +5V: now also C67.1, IC14.6
- net GND: now also C67.2, IC14.3, J1.S2
- net N$48: now also IC14.4
- net N$49: now also IC14.5
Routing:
- net N$6: track 0.00 -> 15.5 mm, vias 0 -> 2
- net N$14: track 0.00 -> 9.93 mm, vias 0 -> 2
- net N$40: track 5.30 -> 0.00 mm
- net N$39: track 5.17 -> 0.00 mm
- net DIN2: track 74.7 -> 69.6 mm
- net N$43: track 7.86 -> 13.0 mm, vias 0 -> 2
- net N$49: track 17.5 -> 21.3 mm
- net UART_RX/DIN1: track 141.7 -> 138.5 mm
- net N$48: track 16.6 -> 19.4 mm, vias 0 -> 2
- net +5V: track 246.0 -> 248.8 mm, vias 11 -> 13
- net +3V3: track 94.5 -> 92.8 mm
- net GND: track 138.4 -> 139.6 mm, vias 144 -> 146
- net N$42: track 4.83 -> 3.82 mm
- net N$47: track 8.40 -> 7.75 mm, vias 2 -> 0
- net UART_TX/DOUT1: track 149.7 -> 150.2 mm
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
